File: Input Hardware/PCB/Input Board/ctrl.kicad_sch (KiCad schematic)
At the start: 0 parts

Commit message: Progress
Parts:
- added C? (x3): 100n, Capacitor_SMD:C_0603_1608Metric, symbol Device:C
- added J?: USB_C_Receptacle_USB2.0_16P, Connector_USB:USB_C_Receptacle_GCT_USB4110, symbol Connector:USB_C_Receptacle_USB2.0_16P
- added JP?: 3.3V STLINK, Jumper:SolderJumper-2_P1.3mm_Open_RoundedPad1.0x1.5mm, symbol Jumper:SolderJumper_2_Open
- added R? (x2): 5.1k, Resistor_SMD:R_0603_1608Metric, symbol Device:R
- added R? (x4): 10k, Resistor_SMD:R_0603_1608Metric, symbol Device:R
- added TP1, TP2, TP3, TP4, TP5: TestPoint, TestPoint:TestPoint_Pad_1.5x1.5mm, symbol Connector:TestPoint
- added U?: STM32F303CBTx, Package_QFP:LQFP-48_7x7mm_P0.5mm, symbol MCU_ST_STM32F3:STM32F303CBTx
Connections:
- new net: JP?.1 (A), TP1.1
- new net: J?.A1 (GND), J?.A12 (GND), J?.B1 (GND), J?.B12 (GND)
- new net: J?.A4 (VBUS), J?.A9 (VBUS), J?.B4 (VBUS), J?.B9 (VBUS)
- new net: J?.A5 (CC1), R?.2
- new net: J?.B5 (CC2), R?.1
- new net: U?.23 (VSS), U?.35 (VSS), U?.47 (VSS)
- new net +3V3: JP?.2 (B), R?.1, R?.1, R?.1
- new net BOOT0: C?.1, R?.1, U?.44 (BOOT0)
- new net GND: C?.2, C?.2, C?.2, R?.1, R?.2, R?.2, TP5.1
- new net NRST: C?.1, R?.2, TP2.1
- new net SWCLK: R?.2, TP3.1
- new net SWDIO: R?.2, TP4.1
- new net USB_DN: J?.A7 (D-), J?.B7 (D-), U?.32 (PA11)
- new net USB_DP: J?.A6 (D+), J?.B6 (D+), U?.33 (PA12)
- new net ~{RST}: C?.1, U?.7 (NRST)
- no-connect marks 0 -> 2

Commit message: WEEEE
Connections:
- net GND: now also J?.A1 (GND), J?.A12 (GND), J?.B1 (GND), J?.B12 (GND), J?.S1 (SHIELD)
- net Rx1: now also U?.13 (PA3)
- net Rx2: now also U?.14 (PA4)
- net Rx3: now also U?.26 (PB13)
- net Rx4: now also U?.27 (PB14)
- net VBUS: now reaches J?.A4 (VBUS), J?.A9 (VBUS), J?.B4 (VBUS), J?.B9 (VBUS)
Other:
- note added: "ADC1_IN4"
- note added: "ADC2_IN1"
- note added: "ADC3_IN5"
- note added: "ADC4_IN4"
- note added: "Level shifting"
- note added: "sort out power"

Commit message: Revert "Merge branch 'main' of https://github.com/seanryder264/HAYES"
This reverts commit bd795aa78e7b7049f2eb147f65c5fdd388d288f7, reversing
changes made to 52c69ad61d85eaec29fd6b5b9781512ece56f4ea.
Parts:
- removed R? (x2): 5.1k, Resistor_SMD:R_0603_1608Metric, symbol Device:R
- removed U?: STM32F303CBTx, Package_QFP:LQFP-48_7x7mm_P0.5mm, symbol MCU_ST_STM32F3:STM32F303CBTx
- added C?: 100n, Capacitor_SMD:C_0603_1608Metric, symbol Device:C
- added R? (x2): 5.1k, Capacitor_SMD:C_0603_1608Metric, symbol Device:R
- added R? (x5): 10k, Resistor_SMD:R_0603_1608Metric, symbol Device:R
- added R?: 1.5k, Resistor_SMD:R_0603_1608Metric, symbol Device:R
- added TP?: TestPoint, TestPoint:TestPoint_Pad_1.5x1.5mm, symbol Connector:TestPoint
- added U?: STM32F303RBTx, Package_QFP:LQFP-64_10x10mm_P0.5mm, symbol MCU_ST_STM32F3:STM32F303RBTx
- added U?: USBLC6-2SC6, Package_TO_SOT_SMD:SOT-23-6, symbol Power_Protection:USBLC6-2SC6
- added Y?: ECS-2520MV-xxx-xx, Oscillator:Oscillator_SMD_ECS_2520MV-xxx-xx-4Pin_2.5x2.0mm, symbol Oscillator:ECS-2520MV-xxx-xx
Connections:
- net NRST is gone; now on net ~{RST}: C?.1, R?.2, TP2.1
- net +3V3: now also C?.1, R?.1, Y?.4 (VDD)
- net BOOT0: now also U?.60 (BOOT0)
- net GND: now also C?.2, R?.2, R?.2, U?.12 (VSSA), U?.2 (GND), U?.31 (VSS), U?.47 (VSS), U?.63 (VSS), Y?.2 (GND)
- net Mux A: now also U?.23 (PA7)
- net Mux B: now also U?.41 (PA8)
- net Mux C: now also U?.42 (PA9)
- net Mux Inhibit: now also U?.43 (PA10)
- net RCLK: now also R?.2, U?.58 (PB6)
- net Rx1: now also U?.17 (PA3), U?.20 (PA4)
- net Rx2: now also U?.26 (PB0), U?.27 (PB1)
- net Rx3: now also U?.21 (PA5), U?.22 (PA6)
- net Rx4: now also U?.30 (PB11), U?.33 (PB12)
- net SDO: now also R?.2, U?.57 (PB5)
- net SRCLK: now also R?.2, U?.55 (PB3)
- net SWCLK: now also U?.49 (PA14)
- net SWDIO: now also U?.46 (PA13)
- net USB_DN: now also U?.44 (PA11), U?.6 (I/O1); no longer J?.A7 (D-), J?.B7 (D-)
- net USB_DP: now also R?.2, U?.4 (I/O2), U?.45 (PA12); no longer J?.A6 (D+), J?.B6 (D+)
- net VBUS: now also U?.5 (VBUS)
- net ~{OE}: now also R?.2, U?.59 (PB7)
- net ~{RST}: now also U?.7 (NRST)
- net ~{SRCLR}: now also R?.2, U?.56 (PB4)
- net USB_CC1: now reaches J?.A5 (CC1)
- net USB_CC1: now also R?.1
- net USB_CC2: now reaches J?.B5 (CC2)
- net USB_CC2: now also R?.1
- new net: J?.A6 (D+), J?.B6 (D+), U?.3 (I/O2)
- new net: J?.A7 (D-), J?.B7 (D-), U?.1 (I/O1)
- new net: TP?.1, Y?.1 (Tri-State)
- new net +5V: R?.1, R?.1, R?.1, R?.1, R?.1
- new net OSC_16M: U?.5 (PF0), Y?.3 (OUT)
- no-connect marks 2 -> 6
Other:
- note added: "ADC2_IN3"
- note added: "ADC3_IN1"
- note added: "ADC4_IN3"
- note added: "COMP3_INM (INVERT)"
- note added: "COMP3_INP (INVERT)"
- note added: "COMP4_INM"
- note added: "COMP4_INP"
- note added: "COMP5_INM (INVERT)"
- note added: "COMP5_INP (INVERT)"
- note added: "COMP6_INM"
- note added: "COMP6_INP"
- note added: "CONNECT 1.65V"
- note added: "SPI1_MOSI"
- note added: "SPI1_SCK"
- note added: "Set IO as open-drain"
- note added: "USB_DM"
- note added: "USB_DP"
- note added: "Use timer 4"
- note removed: "ADC2_IN1"
- note removed: "ADC3_IN5"
- note removed: "ADC4_IN4"
- note removed: "Level shifting"

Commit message: integrate
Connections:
- net 1.65V: now reaches U?.28 (PB2)
- net 1.65V: now also U?.34 (PB13), U?.35 (PB14), U?.36 (PB15)
- net +3V3 renamed +3.3V

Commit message: end me
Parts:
- added C? (x6): 100n, Capacitor_SMD:C_0603_1608Metric, symbol Device:C
- added C?: 10u, Capacitor_SMD:C_0603_1608Metric, symbol Device:C
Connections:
- net +3.3V: now also U?.1 (VBAT), U?.19 (VDD), U?.32 (VDD), U?.48 (VDD), U?.64 (VDD), C?.1, C?.1, C?.1, C?.1, C?.1
- net GND: now also C?.2, C?.2, C?.2, C?.2, C?.2, C?.2, C?.2
- net +3.3VA: now reaches U?.13 (VDDA)
- net +3.3VA: now also C?.1, C?.1
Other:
- note removed: "CONNECT 1.65V"
- note removed: "sort out power"
- moved on the sheet: C?, J?, JP?, R?, TP1, TP2, TP3, TP4, TP5, TP?, U?, Y?

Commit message: minor changes
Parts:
- added TP6: TestPoint, TestPoint:TestPoint_Pad_1.5x1.5mm, symbol Connector:TestPoint
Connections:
- net SRCLK: now also TP6.1
- net +3.3VA renamed VDDA
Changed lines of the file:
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@@
 		)
 	)
+	(wire
+		(pts
+			(xy 76.2 101.6) (xy 71.12 101.6)
+		)
+		(stroke
+			(width 0)
+			(type default)
+		)
+	)
 	(polyline
 		(pts
@@
 		)
 	)
+	(polyline
+		(pts
+			(xy 256.54 93.98) (xy 259.08 93.98)
+		)
+		(stroke
+			(width 0)
+			(type default)
+		)
+	)
 	(wire
 		(pts
@@
 	(wire
 		(pts
-			(xy 69.85 130.81) (xy 69.85 133.35)
+			(xy 69.85 130.81) (xy 69.85 132.08)
 		)
 		(stroke
@@
 		)
 	)
+	(label "TX_SRCLK"
+		(at 71.12 101.6 180)
+		(effects
+			(font
+				(size 1.27 1.27)
+			)
+			(justify right)
+		)
+	)
 	(label "BOOT0"
 		(at 210.82 48.26 180)
@@
 	)
 	(symbol
+		(lib_id "Connector:TestPoint")
+		(at 76.2 101.6 270)
+		(unit 1)
+		(exclude_from_sim no)
+		(in_bom yes)
+		(on_board yes)
+		(dnp no)
+		(property "Reference" "TP6"
+			(at 81.28 101.6 90)
+			(effects
+				(font
+					(size 1.27 1.27)
+				)
+				(justify left)
+			)
+		)
+		(property "Value" "TestPoint"
+			(at 81.28 92.71 90)
+			(effects
+				(font
+					(size 1.27 1.27)
+				)
+				(justify left)
+				(hide yes)
+			)
+		)
+		(property "Footprint" "TestPoint:TestPoint_Pad_1.5x1.5mm"
+			(at 76.2 106.68 0)
+			(effects
+				(font
+					(size 1.27 1.27)
+				)
+				(hide yes)
+			)
+		)
+		(property "Datasheet" "~"
+			(at 76.2 106.68 0)
+			(effects
+				(font
+					(size 1.27 1.27)
+				)
+				(hide yes)
+			)
+		)
+		(property "Description" "test point"
+			(at 76.2 101.6 0)
+			(effects
+				(font
+					(size 1.27 1.27)
+				)
+				(hide yes)
+			)
+		)
+		(pin "1"
+		)
+		(instances
+			(project "Input Board"
+				(path "/198ad8d1-66e3-4deb-889c-1af2b81e67c3/5c16bd2e-d56c-40b8-b84c-f5532d41d46a"
+					(reference "TP6")
+					(unit 1)
+				)
+			)
+		)
+	)
+	(symbol
 		(lib_name "GND_1")
 		(lib_id "power:GND")
@@
 		(lib_name "GND_2")
 		(lib_id "power:GND")
-		(at 69.85 133.35 0)
+		(at 69.85 132.08 0)
 		(unit 1)
 		(exclude_from_sim no)
@@
 		(fields_autoplaced yes)
 		(property "Reference" "#PWR0115"
-			(at 69.85 139.7 0)
+			(at 69.85 138.43 0)
 			(effects
 				(font
@@
 		)
 		(property "Value" "GND"
-			(at 69.85 138.43 0)
+			(at 69.85 137.16 0)
 			(effects
 				(font
@@
 		)
 		(property "Footprint" ""
-			(at 69.85 133.35 0)
+			(at 69.85 132.08 0)
 			(effects
 				(font
@@
 		)
 		(property "Datasheet" ""
-			(at 69.85 133.35 0)
+			(at 69.85 132.08 0)
 			(effects
 				(font
@@
 		)
 		(property "Description" "Power symbol creates a global label with name \"GND\" , ground"
-			(at 69.85 133.35 0)
+			(at 69.85 132.08 0)
 			(effects
 				(font
@@
 			)
 		)
-		(property "Value" "+3.3VA"
-			(at 50.8 172.72 0)
+		(property "Value" "VDDA"
+			(at 53.34 176.5299 0)
 			(effects
 				(font
 					(size 1.27 1.27)
 				)
+				(justify left)
 			)
 		)
@@
 			)
 		)
-		(property "Value" "+3.3VA"
+		(property "Value" "VDDA"
 			(at 236.22 33.02 90)
 			(effects

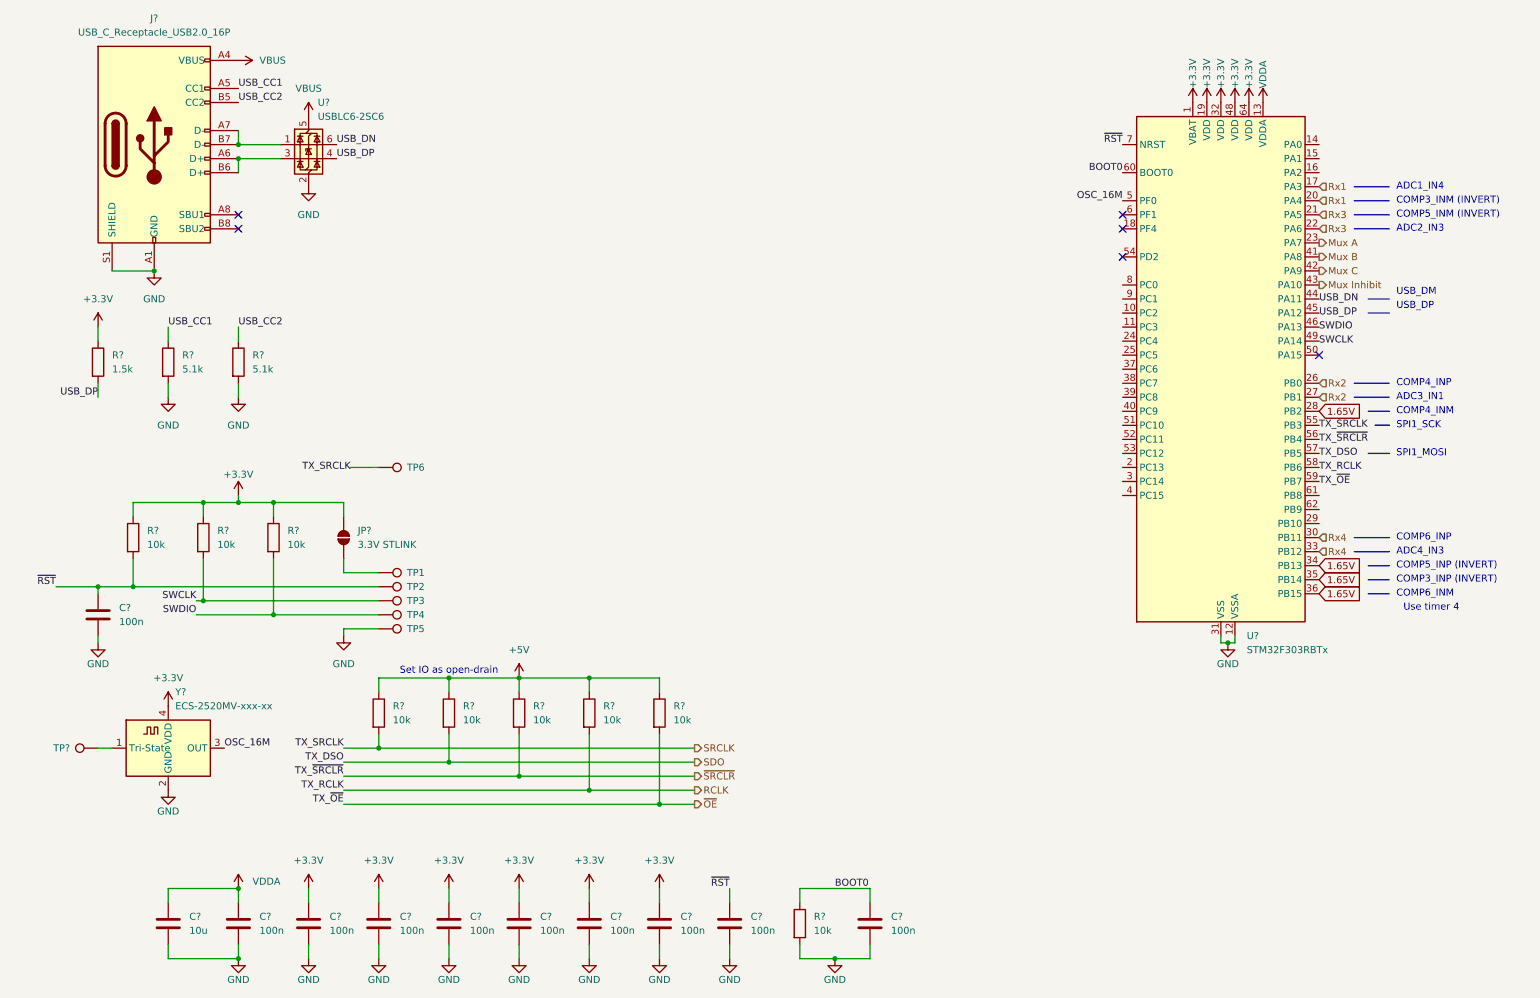
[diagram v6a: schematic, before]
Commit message: input encoder and LEDs
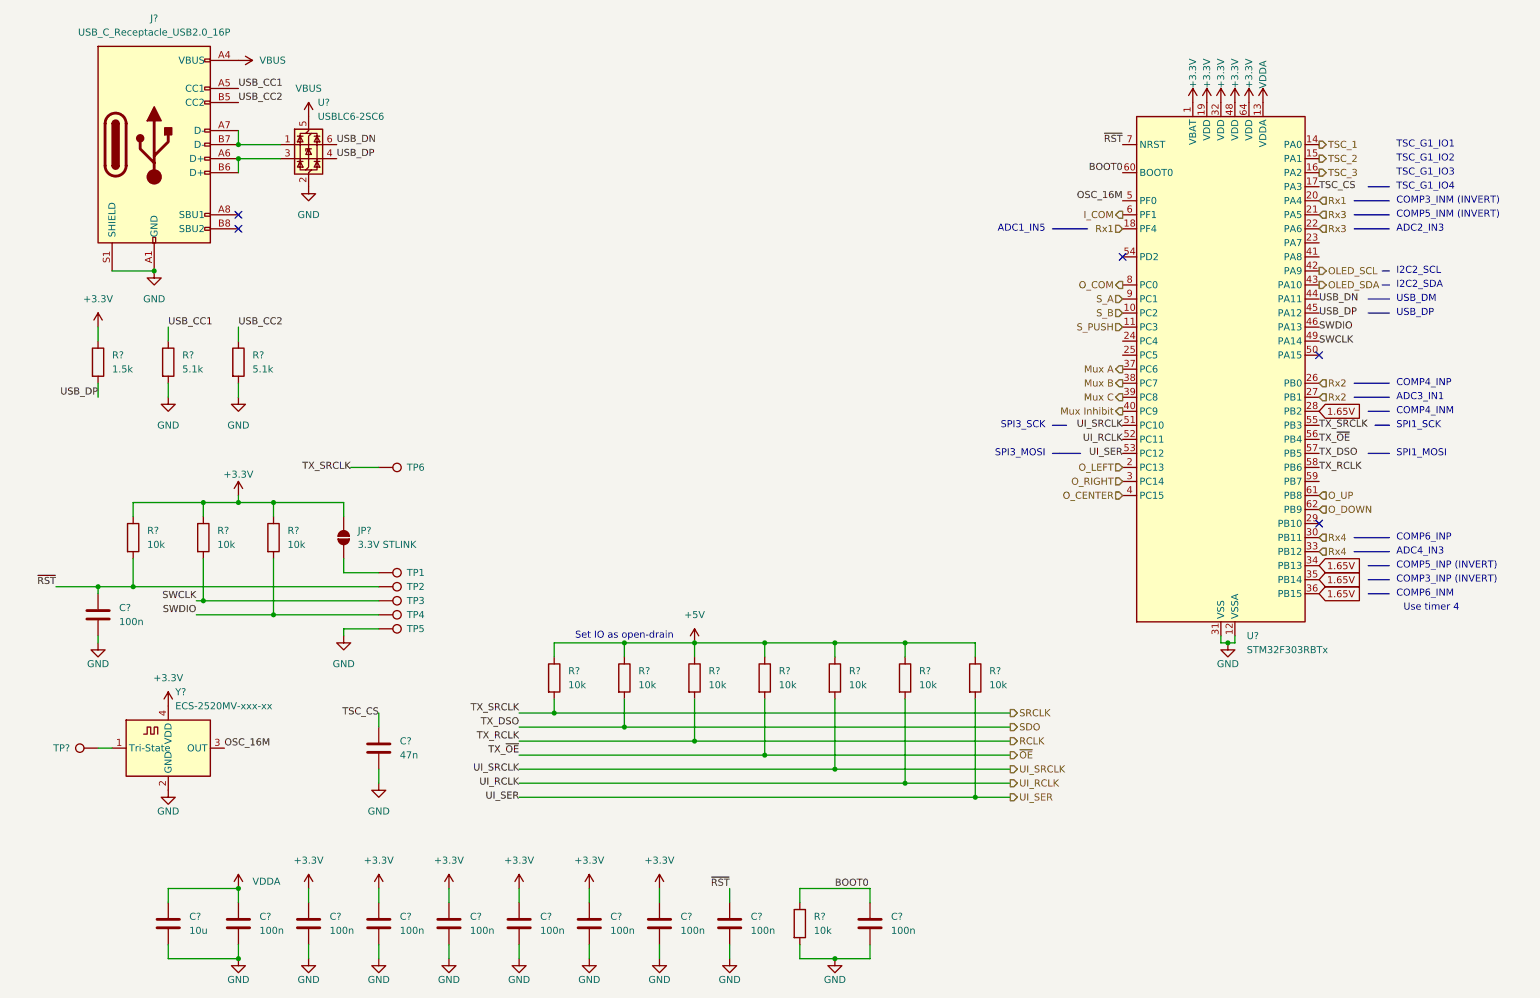
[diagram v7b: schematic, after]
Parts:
- removed R?: 10k, Resistor_SMD:R_0603_1608Metric, symbol Device:R
- added C?: 47n, Capacitor_SMD:C_0603_1608Metric, symbol Device:C
- added R? (x3): 10k, Resistor_SMD:R_0603_1608Metric, symbol Device:R
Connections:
- net ~{SRCLR} is gone; now on net ~{OE}: U?.56 (PB4)
- net +5V: now also R?.1, R?.1, R?.1
- net GND: now also C?.2
- net Mux A: now also U?.37 (PC6); no longer U?.23 (PA7)
- net Mux B: now also U?.38 (PC7); no longer U?.41 (PA8)
- net Mux C: now also U?.39 (PC8); no longer U?.42 (PA9)
- net Mux Inhibit: now also U?.40 (PC9); no longer U?.43 (PA10)
- net RCLK: now also R?.2; no longer R?.2
- net Rx1: now also U?.18 (PF4); no longer U?.17 (PA3)
- net ~{OE}: now also R?.2; no longer R?.2, U?.59 (PB7)
- net S_B: now reaches U?.10 (PC2)
- net S_PUSH: now reaches U?.11 (PC3)
- net TSC_1: now reaches U?.14 (PA0)
- net TSC_2: now reaches U?.15 (PA1)
- net TSC_3: now reaches U?.16 (PA2)
- net O_LEFT: now reaches U?.2 (PC13)
- net O_RIGHT: now reaches U?.3 (PC14)
- net O_CENTER: now reaches U?.4 (PC15)
- net UI_SRCLK: now reaches U?.51 (PC10)
- net UI_SRCLK: now also R?.2
- net UI_RCLK: now reaches U?.52 (PC11)
- net UI_RCLK: now also R?.2
- net UI_SER: now reaches U?.53 (PC12)
- net UI_SER: now also R?.2
- net I_COM: now reaches U?.6 (PF1)
- net O_UP: now reaches U?.61 (PB8)
- net O_DOWN: now reaches U?.62 (PB9)
- net O_COM: now reaches U?.8 (PC0)
- net S_A: now reaches U?.9 (PC1)
- new net OLED_SCL: U?.42 (PA9)
- new net OLED_SDA: U?.43 (PA10)
- new net TSC_CS: C?.1, U?.17 (PA3)
- no-connect marks 6 -> 5
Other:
- note added: "ADC1_IN5"
- note added: "I2C2_SCL"
- note added: "I2C2_SDA"
- note added: "SPI3_MOSI"
- note added: "SPI3_SCK"
- note added: "TSC_G1_IO1"
- note added: "TSC_G1_IO2"
- note added: "TSC_G1_IO3"
- note added: "TSC_G1_IO4"
- note removed: "ADC1_IN4"
- moved on the sheet: R?
